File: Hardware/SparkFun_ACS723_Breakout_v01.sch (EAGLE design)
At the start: 19 parts, among them J1 455-1750-1-ND, U1 ACS723

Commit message: changes after v01
-adjusted pin label font form 32mil to 40mil
-changed standoff to a part that lives in the sparkfun-hardware lbr
-adjusted some spacing on silk labels
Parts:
- JP3: value STAND-OFFTIGHTER_(0.11_INCH_DIA) -> STAND-OFFTIGHT; device Testing:STAND-OFFTIGHTER_(0.11_INCH_DIA) -> SparkFun-Hardware:STAND-OFFTIGHT
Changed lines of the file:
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@@
 <part name="FRAME1" library="SparkFun-Aesthetics" deviceset="FRAME-LETTER" device=""/>
 <part name="J1" library="SparkFun-Connectors" deviceset="CONN_03" device="" value="455-1750-1-ND"/>
-<part name="JP3" library="Testing" deviceset="STAND-OFF" device="TIGHTER_(0.11_INCH_DIA)"/>
+<part name="JP3" library="SparkFun-Hardware" deviceset="STAND-OFF" device="TIGHT"/>
 <part name="LOGO1" library="SparkFun-Aesthetics" deviceset="SFE_LOGO_FLAME" device=".1_INCH"/>
 <part name="LOGO3" library="SparkFun-Aesthetics" deviceset="SFE_LOGO_NAME_FLAME" device=".1_INCH"/>

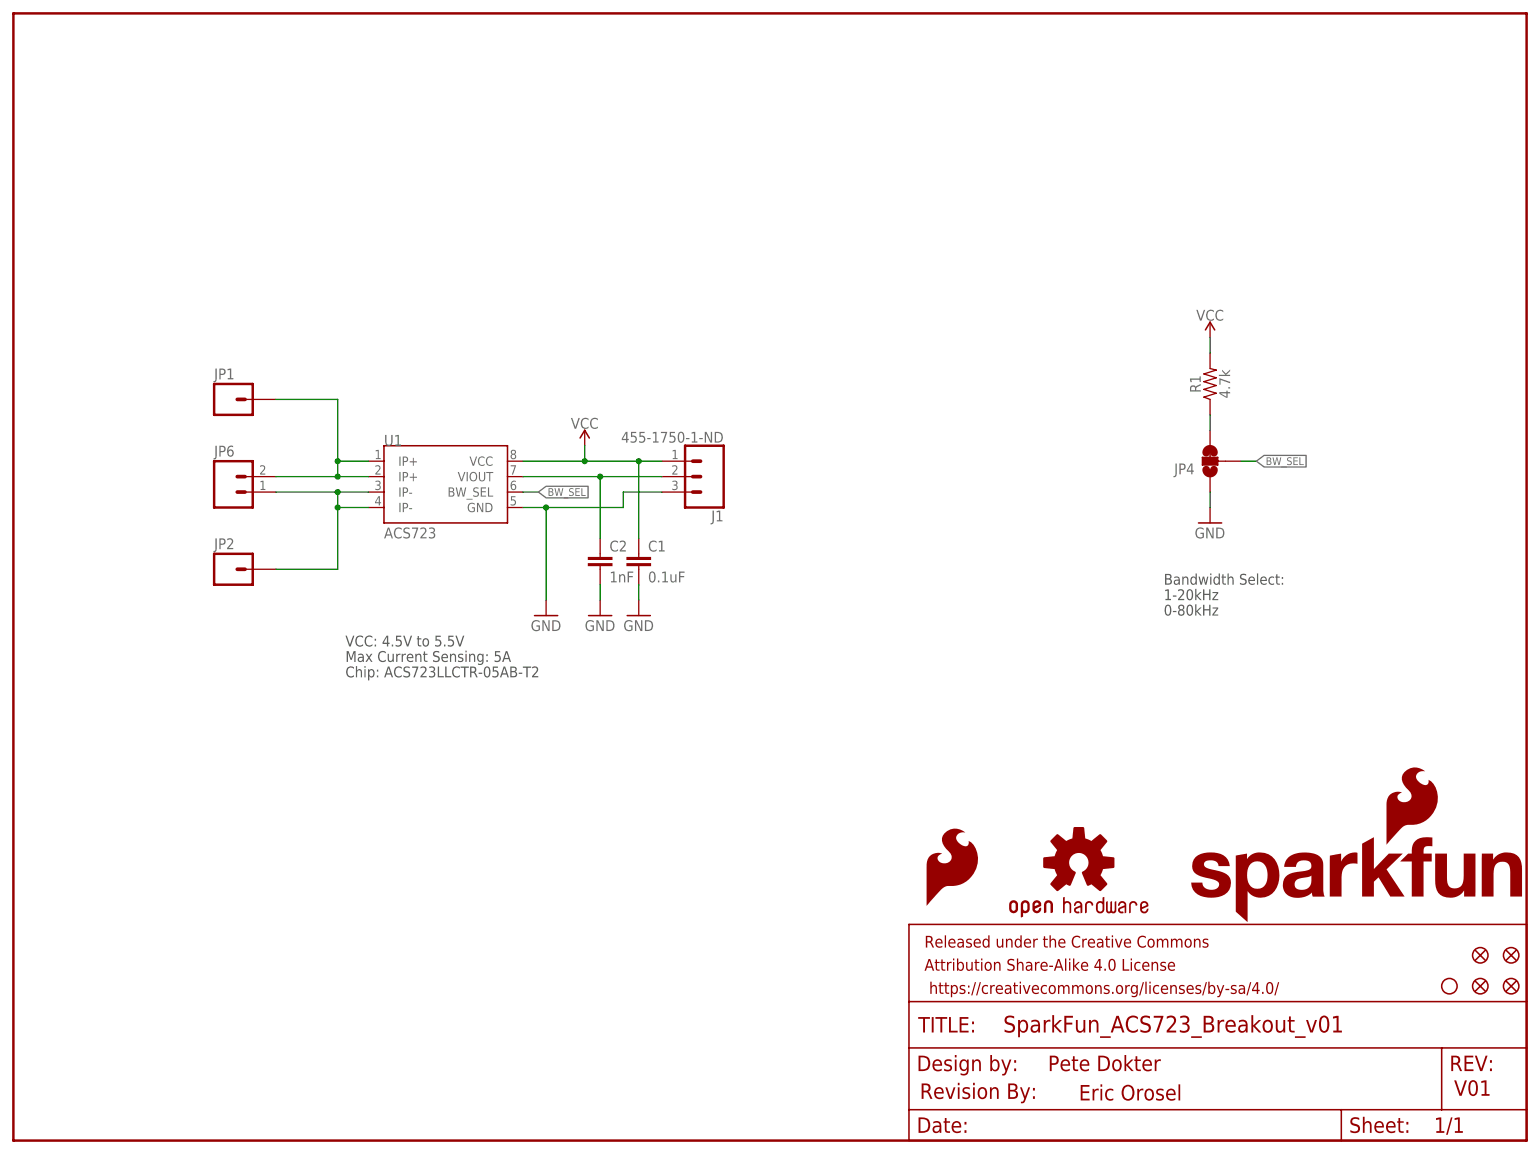
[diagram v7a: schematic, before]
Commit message: v01 to v10 finalization
-added notes for bandwidth select
-added full IC name
-added small info partition in sch
-changed version numbers from v01 to v10
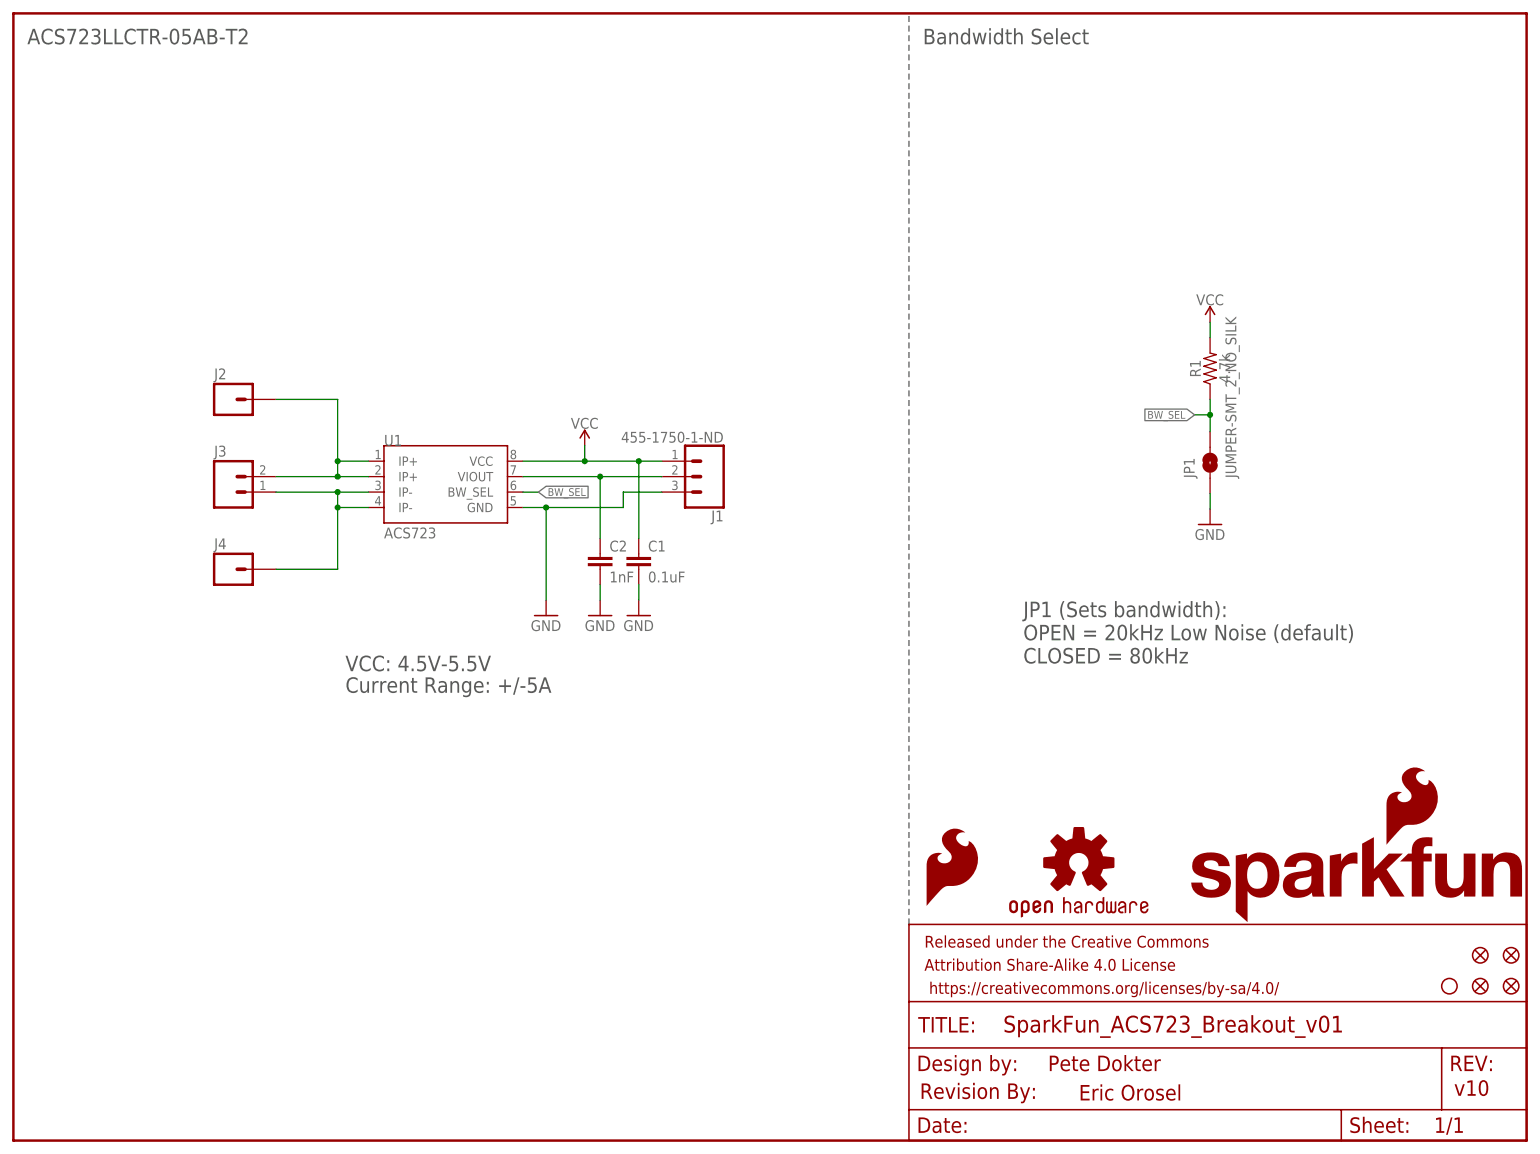
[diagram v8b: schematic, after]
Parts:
- removed JP4: JUMPER-SMT_3_1-NC_TRACE_SILK, SparkFun-Jumpers:JUMPER-SMT_3_1-NC_TRACE_SILK
- added J2: (no value), SparkFun-Connectors:M01-SMTSO-256-ET
- JP1: value (none) -> JUMPER-SMT_2_NO_SILK; device SparkFun-Connectors:M01-SMTSO-256-ET -> SparkFun-Jumpers:JUMPER-SMT_2_NO_SILK
- renumbered JP2 to J4, JP6 to J3
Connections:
- removed net N$3: JP4.3, R1.1
- net BW_SEL: now also JP1.2, R1.1; no longer JP4.2
- net GND: now also JP1.1; no longer JP4.1
- net IP+: now also J2.1; no longer JP1.1
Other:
- note added: "ACS723LLCTR-05AB-T2"
- note added: "Bandwidth Select"
- note added: "CLOSED = 80kHz"
- note added: "Current Range: +/-5A"
- note added: "JP1 (Sets bandwidth):"
- note added: "OPEN = 20kHz Low Noise (default)"
- note added: "VCC: 4.5V-5.5V"
- note added: "v10"
- note removed: "0-80kHz"
- note removed: "1-20kHz"
- note removed: "Bandwidth Select:"
- note removed: "Chip: ACS723LLCTR-05AB-T2"
- note removed: "Max Current Sensing: 5A"
- note removed: "V01"
- note removed: "VCC: 4.5V to 5.5V"
- moved on the sheet: JP1, R1
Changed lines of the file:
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@@
 </classes>
 <parts>
-<part name="JP1" library="SparkFun-Connectors" deviceset="M01" device="-SMTSO-256-ET"/>
-<part name="JP2" library="SparkFun-Connectors" deviceset="M01" device="-SMTSO-256-ET"/>
-<part name="JP6" library="SparkFun-Connectors" deviceset="M02" device="1X02_NO_SILK"/>
+<part name="J2" library="SparkFun-Connectors" deviceset="M01" device="-SMTSO-256-ET"/>
+<part name="J4" library="SparkFun-Connectors" deviceset="M01" device="-SMTSO-256-ET"/>
+<part name="J3" library="SparkFun-Connectors" deviceset="M02" device="1X02_NO_SILK"/>
 <part name="SUPPLY1" library="SparkFun-PowerSymbols" deviceset="VCC" device=""/>
 <part name="GND1" library="SparkFun-Aesthetics" deviceset="GND" device=""/>
@@
 <part name="FD4" library="SparkFun-Aesthetics" deviceset="FIDUCIAL" device="1X2"/>
 <part name="FD5" library="SparkFun-Aesthetics" deviceset="FIDUCIAL" device="1X2"/>
-<part name="JP4" library="SparkFun-Jumpers" deviceset="JUMPER-SMT_3_1-NC_TRACE" device="_SILK"/>
 <part name="GND4" library="SparkFun-Aesthetics" deviceset="GND" device=""/>
 <part name="R1" library="SparkFun-Resistors" deviceset="4.7KOHM" device="-0603-1/10W-1%" value="4.7k"/>
@@
 <part name="LOGO3" library="SparkFun-Aesthetics" deviceset="SFE_LOGO_NAME_FLAME" device=".1_INCH"/>
 <part name="LOGO4" library="SparkFun-Aesthetics" deviceset="OSHW-LOGO" device="M"/>
+<part name="JP1" library="SparkFun-Jumpers" deviceset="JUMPER-SMT_2_NO" device="_SILK"/>
 </parts>
 <sheets>
@@
 <plain>
 <text x="170.18" y="11.43" size="2.54" layer="94">Pete Dokter</text>
-<text x="236.982" y="7.366" size="2.54" layer="94">V01</text>
+<text x="236.982" y="7.366" size="2.54" layer="94">v10</text>
 <text x="175.26" y="6.604" size="2.54" layer="94">Eric Orosel</text>
-<text x="54.61" y="78.74" size="1.778" layer="97">Max Current Sensing: 5A</text>
-<text x="54.61" y="81.28" size="1.778" layer="97">VCC: 4.5V to 5.5V</text>
-<text x="54.61" y="76.2" size="1.778" layer="97">Chip: ACS723LLCTR-05AB-T2</text>
-<text x="189.23" y="91.44" size="1.778" layer="97">Bandwidth Select:</text>
-<text x="189.23" y="88.9" size="1.778" layer="97">1-20kHz</text>
-<text x="189.23" y="86.36" size="1.778" layer="97">0-80kHz</text>
+<text x="54.61" y="73.66" size="2.54" layer="97">Current Range: +/-5A</text>
+<text x="54.61" y="77.216" size="2.54" layer="97">VCC: 4.5V-5.5V</text>
+<text x="166.116" y="86.106" size="2.54" layer="97">JP1 (Sets bandwidth):</text>
+<text x="166.116" y="78.486" size="2.54" layer="97">CLOSED = 80kHz</text>
+<text x="166.116" y="82.296" size="2.54" layer="97">OPEN = 20kHz Low Noise (default)</text>
+<wire x1="147.32" y1="35.56" x2="147.32" y2="185.42" width="0.2032" layer="97" style="shortdash"/>
+<text x="2.286" y="180.34" size="2.54" layer="97">ACS723LLCTR-05AB-T2</text>
+<text x="149.606" y="180.34" size="2.54" layer="97">Bandwidth Select</text>
 </plain>
 <instances>
-<instance part="JP1" gate="G$1" x="35.56" y="121.92"/>
-<instance part="JP2" gate="G$1" x="35.56" y="93.98"/>
-<instance part="JP6" gate="G$1" x="35.56" y="106.68"/>
+<instance part="J2" gate="G$1" x="35.56" y="121.92"/>
+<instance part="J4" gate="G$1" x="35.56" y="93.98"/>
+<instance part="J3" gate="G$1" x="35.56" y="106.68"/>
 <instance part="SUPPLY1" gate="G$1" x="93.98" y="114.3"/>
 <instance part="GND1" gate="1" x="87.63" y="86.36"/>
@@
 <instance part="FD4" gate="G$1" x="241.3" y="25.4"/>
 <instance part="FD5" gate="G$1" x="246.38" y="25.4"/>
-<instance part="JP4" gate="G$1" x="196.85" y="111.76" smashed="yes" rot="R180">
-<attribute name="NAME" x="194.31" y="111.379" size="1.778" layer="95" font="vector" rot="R180"/>
-</instance>
-<instance part="GND4" gate="1" x="196.85" y="101.6"/>
-<instance part="R1" gate="G$1" x="196.85" y="124.46" rot="R90"/>
-<instance part="SUPPLY2" gate="G$1" x="196.85" y="132.08"/>
+<instance part="GND4" gate="1" x="196.85" y="101.346"/>
+<instance part="R1" gate="G$1" x="196.85" y="127" rot="R90"/>
+<instance part="SUPPLY2" gate="G$1" x="196.85" y="134.62"/>
 <instance part="C2" gate="G$1" x="96.52" y="93.98"/>
 <instance part="GND3" gate="1" x="96.52" y="86.36"/>
@@
 <instance part="LOGO3" gate="G$1" x="193.04" y="35.56"/>
 <instance part="LOGO4" gate="G$1" x="175.26" y="45.72"/>
+<instance part="JP1" gate="G$1" x="196.85" y="111.506" rot="R90"/>
 </instances>
 <busses>
@@
 <wire x1="53.34" y1="109.22" x2="53.34" y2="111.76" width="0.1524" layer="91"/>
 <junction x="53.34" y="111.76"/>
-<pinref part="JP1" gate="G$1" pin="1"/>
-<pinref part="JP6" gate="G$1" pin="2"/>
+<pinref part="J2" gate="G$1" pin="1"/>
+<pinref part="J3" gate="G$1" pin="2"/>
 <wire x1="43.18" y1="109.22" x2="53.34" y2="109.22" width="0.1524" layer="91"/>
 <junction x="53.34" y="109.22"/>
@@
 <wire x1="58.42" y1="104.14" x2="53.34" y2="104.14" width="0.1524" layer="91"/>
 <junction x="53.34" y="104.14"/>
-<pinref part="JP2" gate="G$1" pin="1"/>
-<pinref part="JP6" gate="G$1" pin="1"/>
+<pinref part="J4" gate="G$1" pin="1"/>
+<pinref part="J3" gate="G$1" pin="1"/>
 <wire x1="43.18" y1="106.68" x2="53.34" y2="106.68" width="0.1524" layer="91"/>
 <junction x="53.34" y="106.68"/>
@@
 <segment>
 <pinref part="R1" gate="G$1" pin="2"/>
-<wire x1="196.85" y1="129.54" x2="196.85" y2="132.08" width="0.1524" layer="91"/>
+<wire x1="196.85" y1="132.08" x2="196.85" y2="134.62" width="0.1524" layer="91"/>
 <pinref part="SUPPLY2" gate="G$1" pin="VCC"/>
 </segment>
@@
 </segment>
 <segment>
-<pinref part="JP4" gate="G$1" pin="1"/>
-<wire x1="196.85" y1="106.68" x2="196.85" y2="104.14" width="0.1524" layer="91"/>
-<pinref part="GND4" gate="1" pin="GND"/>
-</segment>
-<segment>
 <pinref part="C2" gate="G$1" pin="2"/>
 <wire x1="96.52" y1="91.44" x2="96.52" y2="88.9" width="0.1524" layer="91"/>
 <pinref part="GND3" gate="1" pin="GND"/>
+</segment>
+<segment>
+<pinref part="GND4" gate="1" pin="GND"/>
+<pinref part="JP1" gate="G$1" pin="1"/>
+<wire x1="196.85" y1="103.886" x2="196.85" y2="106.426" width="0.1524" layer="91"/>
 </segment>
 </net>
@@
 </segment>
 <segment>
-<pinref part="JP4" gate="G$1" pin="2"/>
-<wire x1="201.93" y1="111.76" x2="204.47" y2="111.76" width="0.1524" layer="91"/>
-<label x="204.47" y="111.76" size="1.27" layer="95" xref="yes"/>
+<wire x1="196.85" y1="119.38" x2="194.31" y2="119.38" width="0.1524" layer="91"/>
+<label x="194.31" y="119.38" size="1.27" layer="95" rot="R180" xref="yes"/>
+<pinref part="R1" gate="G$1" pin="1"/>
+<wire x1="196.85" y1="121.92" x2="196.85" y2="119.38" width="0.1524" layer="91"/>
+<pinref part="JP1" gate="G$1" pin="2"/>
+<wire x1="196.85" y1="119.38" x2="196.85" y2="116.586" width="0.1524" layer="91"/>
+<junction x="196.85" y="119.38"/>
 </segment>
 </net>
-<net name="N$3" class="3">
-<segment>
-<pinref part="JP4" gate="G$1" pin="3"/>
-<wire x1="196.85" y1="116.84" x2="196.85" y2="119.38" width="0.1524" layer="91"/>
-<pinref part="R1" gate="G$1" pin="1"/>
-</segment>
-</net>
